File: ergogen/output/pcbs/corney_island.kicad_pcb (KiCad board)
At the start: 2 copper layers, 134.2 x 92.7 mm, 67 parts

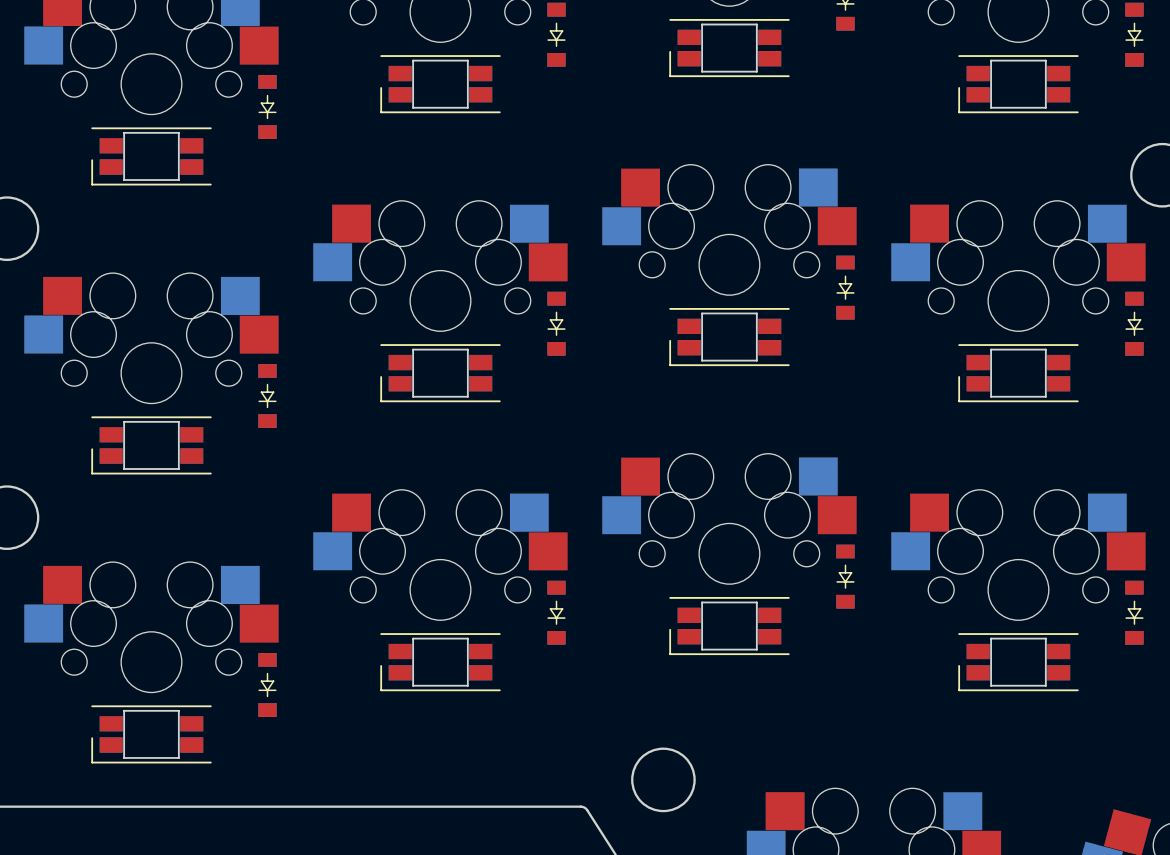
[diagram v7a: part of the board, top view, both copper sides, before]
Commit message: Add underglow LEDs
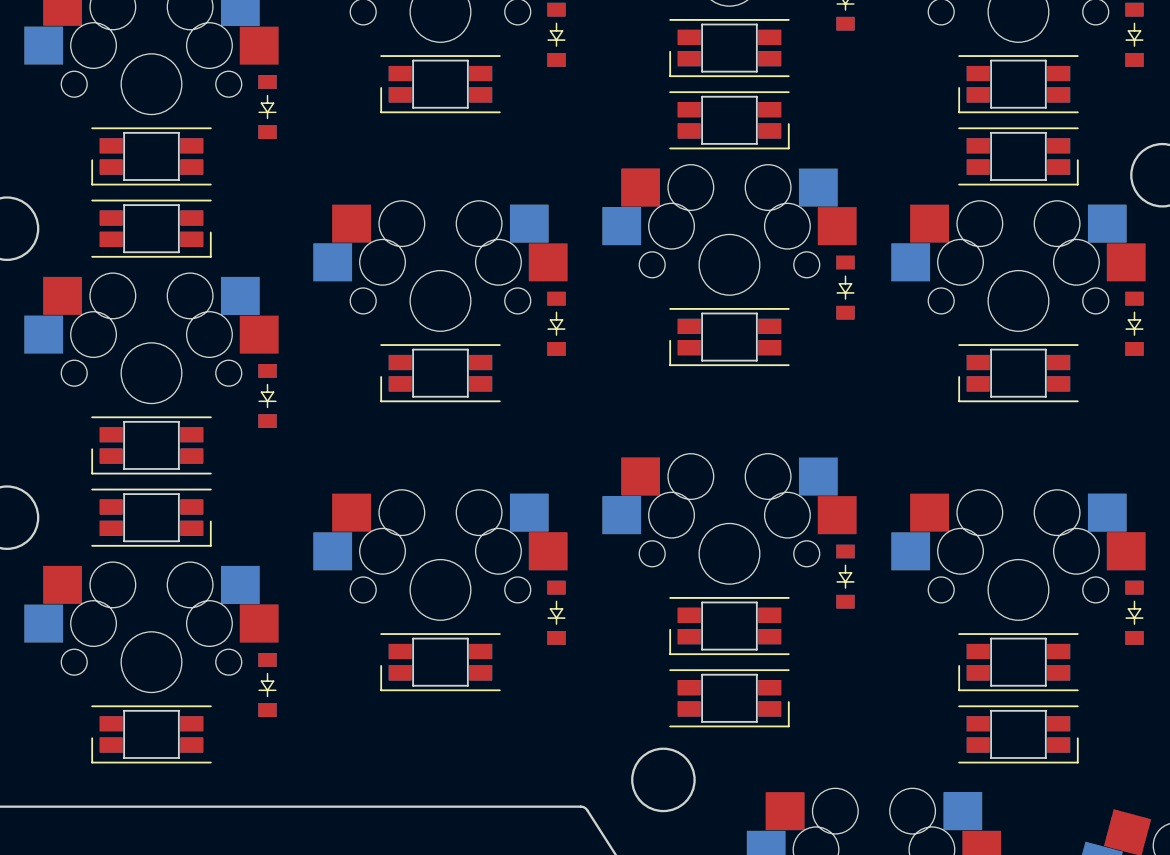
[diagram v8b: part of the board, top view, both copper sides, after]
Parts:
- added LED23: YS-SK6812MINI-E, YS-SK6812MINI-E, F.Cu at (119.0, 71.5)
- added LED24: YS-SK6812MINI-E, YS-SK6812MINI-E, F.Cu at (157.0, 102.4)
- added LED25: YS-SK6812MINI-E, YS-SK6812MINI-E, F.Cu at (157.0, 64.4)
- added LED26: YS-SK6812MINI-E, YS-SK6812MINI-E, F.Cu at (176.0, 104.8)
- added LED27: YS-SK6812MINI-E, YS-SK6812MINI-E, F.Cu at (176.0, 66.8)
- added LED28: , combo_display, F.Cu at (214.6, 91.2)
- LED22: value combined_oled -> YS-SK6812MINI-E; footprint combined_oled -> YS-SK6812MINI-E
- moved LED22 95.6 mm to (119.0, 90.5)
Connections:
- LED10 pad 2: LED_11 -> ULED_3
- LED12 pad 2: LED_9 -> ULED_2
- LED13 pad 4: LED_5 -> ULED_5
- LED15 pad 4: LED_7 -> ULED_6
- LED22 pad 1: GND -> VCC
- LED22 pad 2: VCC -> LED_17
- LED22 pad 3: SCL -> GND
- LED22 pad 4: SDA -> ULED_0
- LED5 pad 2: LED_17 -> ULED_0
- LED6 pad 2: LED_16 -> ULED_1
